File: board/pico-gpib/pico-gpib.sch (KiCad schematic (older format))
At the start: 5 parts, among them J1 GPIB, J2 USB_B_Micro, J3 RPI_GPIO, U2 SN75160BDW, U3 SN75162BDW

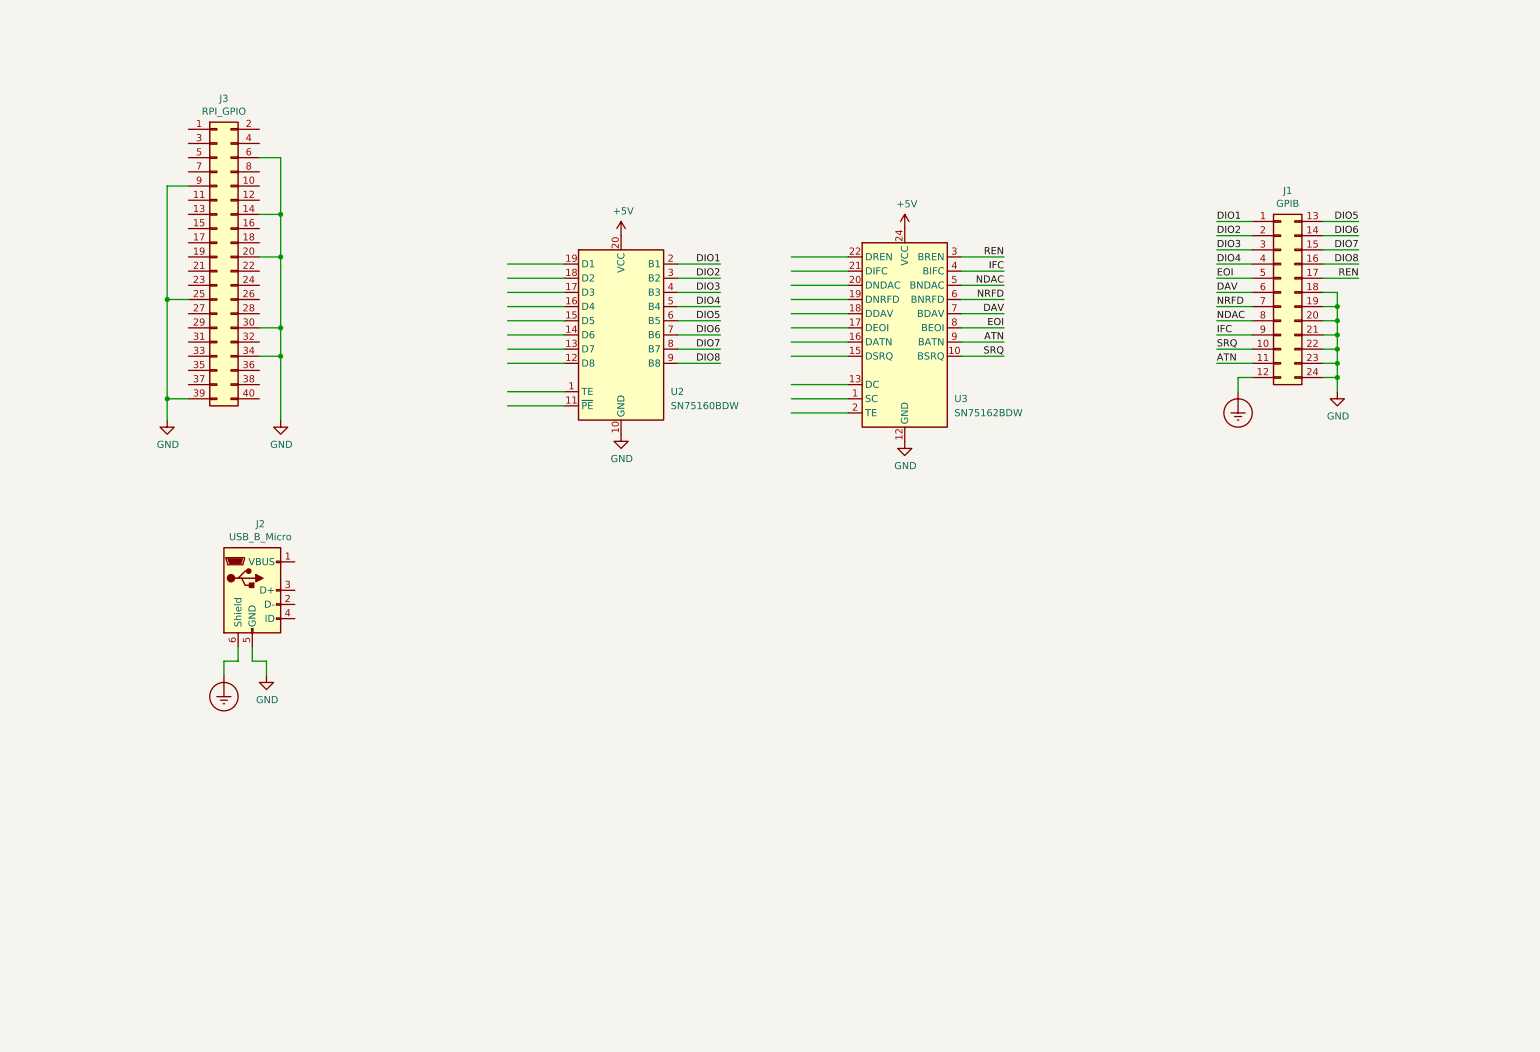
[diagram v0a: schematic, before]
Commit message: Swap connectors to top of pico board.
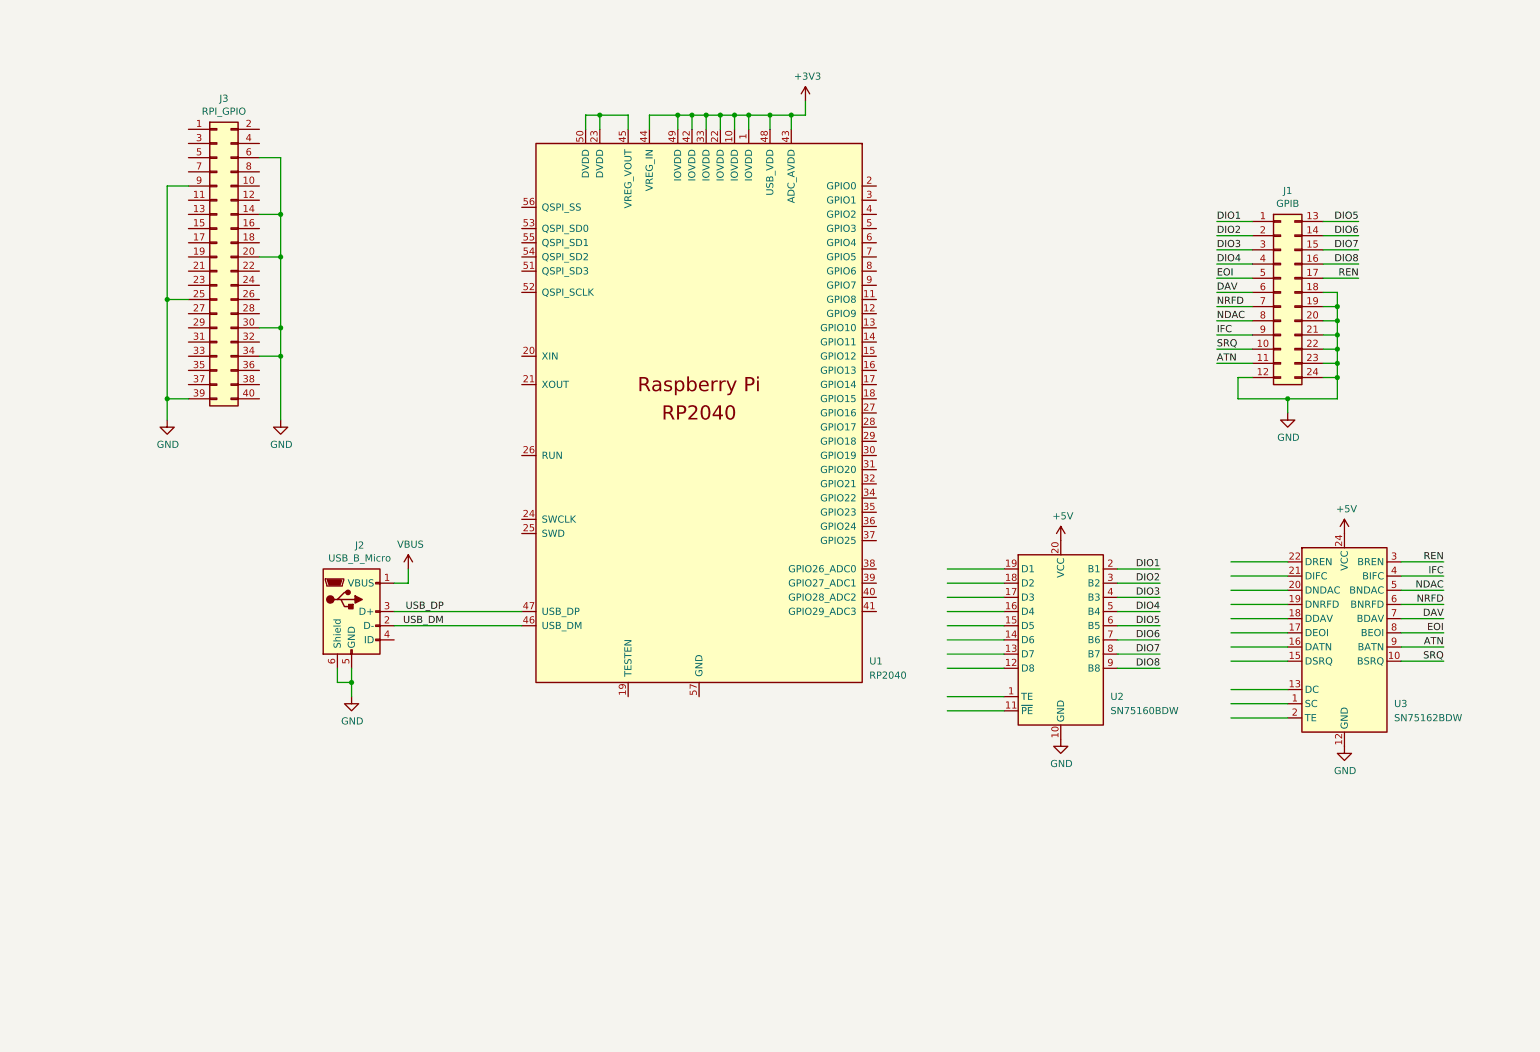
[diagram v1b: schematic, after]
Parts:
- added U1: RP2040, local:RP2040-QFN-56, symbol local:RP2040
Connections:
- net labels added: +3V3, USB_DM, USB_DP, VBUS
- net labels removed: Earth_Protective
- wire segments 91 -> 120
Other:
- moved on the sheet: J2, U2, U3

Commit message: Place and route most of the pico board.
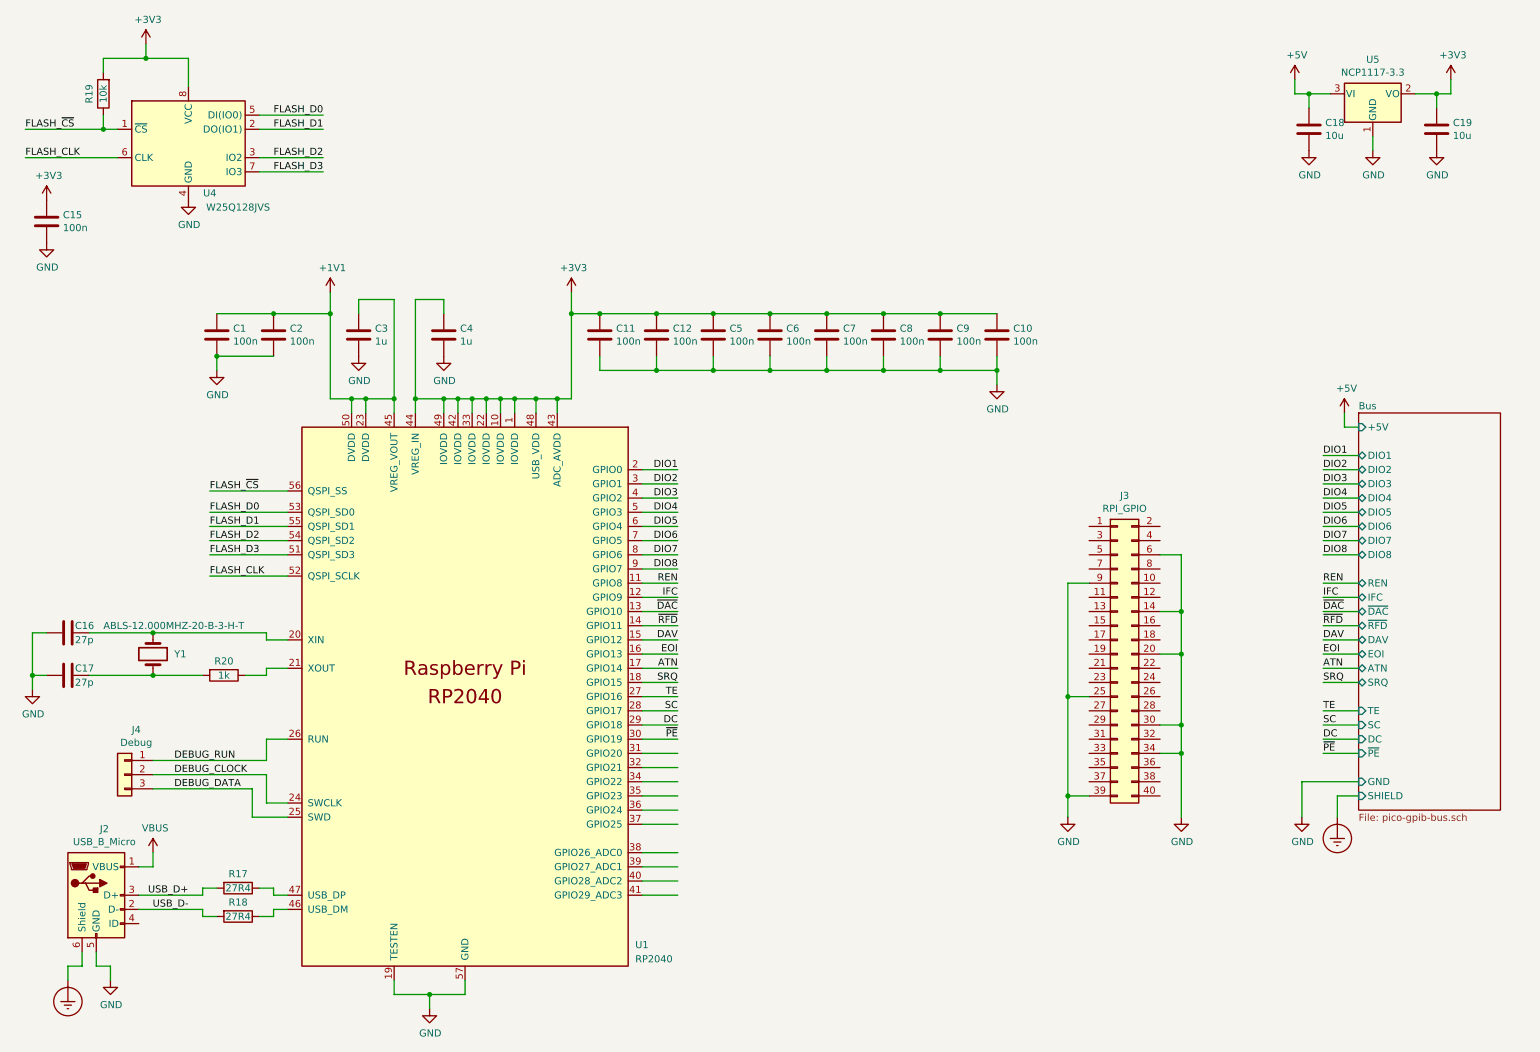
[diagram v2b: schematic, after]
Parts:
- removed J1: GPIB, local:NorComp_112-024-113R001, symbol Connector_Generic:Conn_02x12_Top_Bottom
- removed U2: SN75160BDW, Package_SO:SOIC-20W_7.5x12.8mm_P1.27mm, symbol Interface:SN75160BDW
- removed U3: SN75162BDW, Package_SO:SOIC-24W_7.5x15.4mm_P1.27mm, symbol local:SN75162BDW
- added C1, C10, C11, C12, C15, C2, C5, C6, C7, C8, C9: 100n, Capacitor_SMD:C_0402_1005Metric, symbol Device:C
- added C16, C17: 27p, Capacitor_SMD:C_0402_1005Metric, symbol Device:C
- added C18, C19: 10u, Capacitor_SMD:C_0402_1005Metric, symbol Device:C
- added C3, C4: 1u, Capacitor_SMD:C_0402_1005Metric, symbol Device:C
- added J4: Debug, Connector_PinHeader_2.54mm:PinHeader_1x03_P2.54mm_Horizontal, symbol Connector_Generic:Conn_01x03
- added R17, R18: 27R4, Resistor_SMD:R_0402_1005Metric, symbol Device:R
- added R19: 10k, Resistor_SMD:R_0402_1005Metric, symbol Device:R
- added R20: 1k, Resistor_SMD:R_0402_1005Metric, symbol Device:R
- added U4: W25Q128JVS, Package_SO:SOIC-8_5.23x5.23mm_P1.27mm, symbol Memory_Flash:W25Q128JVS
- added U5: NCP1117-3.3, Package_TO_SOT_SMD:SOT-223-3_TabPin2, symbol Regulator_Linear:NCP1117-3.3_SOT223
- added Y1: ABLS-12.000MHZ-20-B-3-H-T, Crystal:Crystal_HC49-U_Horizontal, symbol Device:Crystal
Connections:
- net labels added: +1V1, DC, DEBUG_CLOCK, DEBUG_DATA, DEBUG_RUN, Earth_Protective, FLASH_CLK, FLASH_D0, FLASH_D1, FLASH_D2, FLASH_D3, FLASH_~CS, SC, TE, USB_D+, USB_D-, ~DAC, ~PE, ~RFD
- net labels removed: NDAC, NRFD, USB_DM, USB_DP
- wire segments 120 -> 209
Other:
- moved on the sheet: J2, J3, U1

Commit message: Rotate RP2040 to fit in crystal.
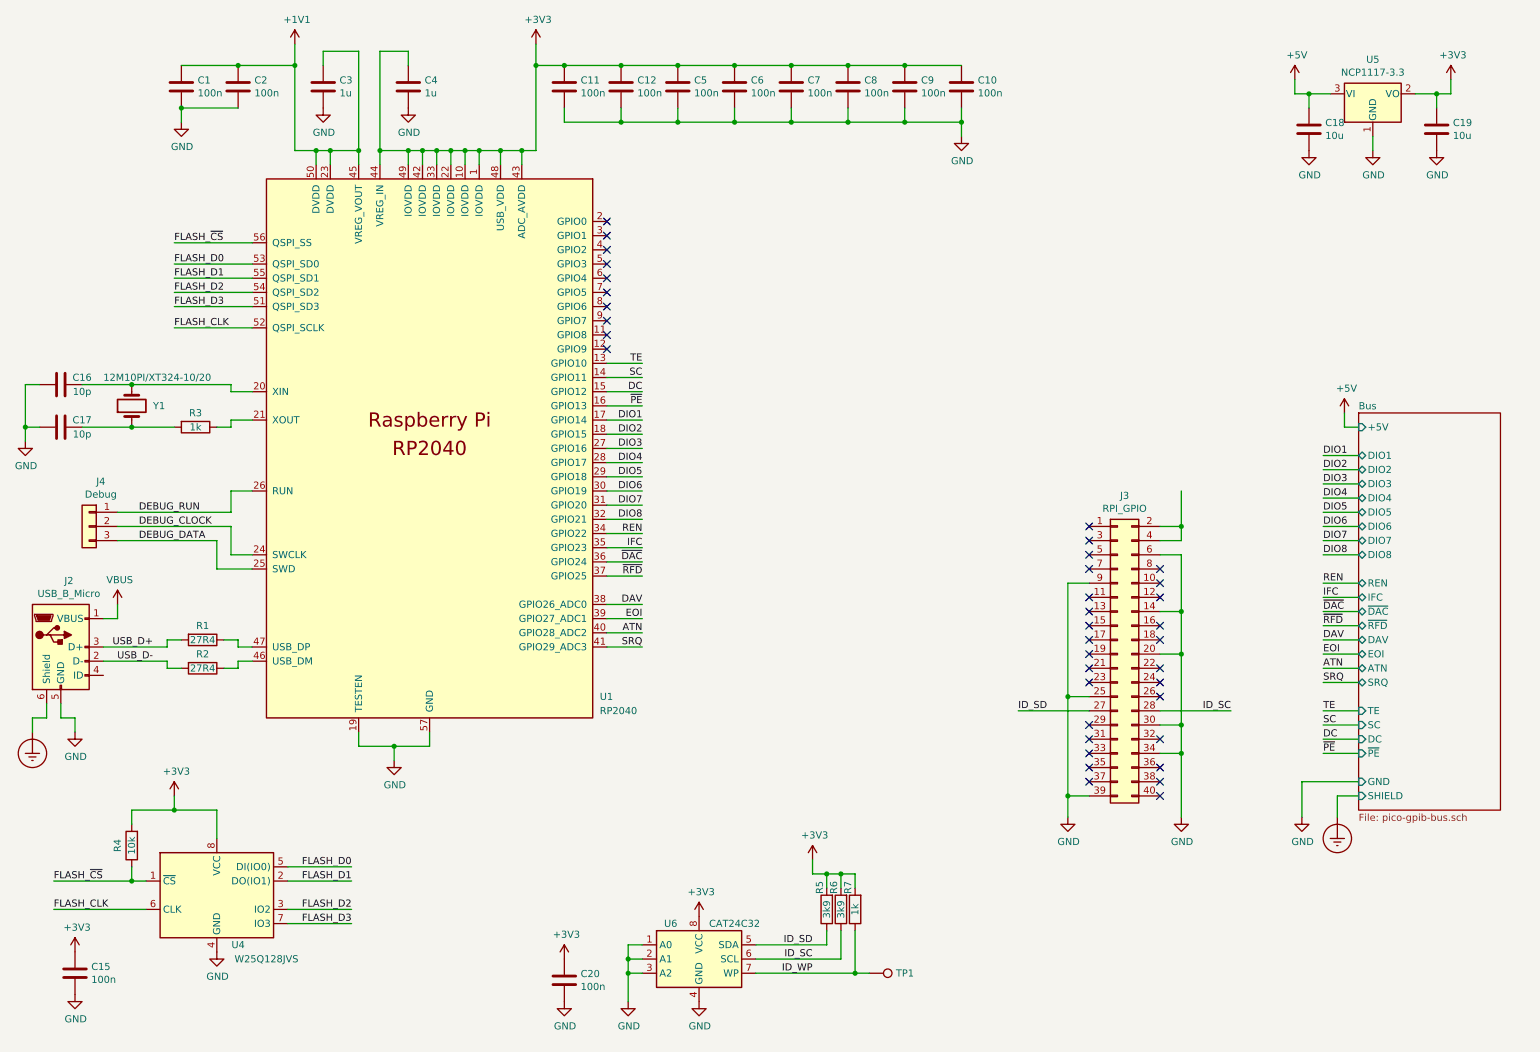
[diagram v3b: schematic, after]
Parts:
- removed R20: 1k, Resistor_SMD:R_0402_1005Metric, symbol Device:R
- added C20: 100n, Capacitor_SMD:C_0402_1005Metric, symbol Device:C
- added R3, R7: 1k, Resistor_SMD:R_0402_1005Metric, symbol Device:R
- added R5, R6: 3k9, Resistor_SMD:R_0402_1005Metric, symbol Device:R
- added TP1: TestPoint, TestPoint:TestPoint_Pad_D1.0mm, symbol Connector:TestPoint
- added U6: CAT24C32, Package_SO:SOIC-8_3.9x4.9mm_P1.27mm, symbol Memory_EEPROM:CAT24C128
- C16, C17: value 27p -> 10p
- J4: footprint Connector_PinHeader_2.54mm:PinHeader_1x03_P2.54mm_Horizontal -> Connector_PinHeader_2.54mm:PinHeader_1x03_P2.54mm_Vertical
- Y1: value ABLS-12.000MHZ-20-B-3-H-T -> 12M10PI/XT324-10/20; footprint Crystal:Crystal_HC49-U_Horizontal -> Crystal:Crystal_SMD_3225-4Pin_3.2x2.5mm
- renumbered R17 to R1, R18 to R2, R19 to R4
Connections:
- net labels added: ID_SC, ID_SD, ID_WP
- wire segments 209 -> 225
- no-connect marks 0 -> 38
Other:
- moved on the sheet: C1, C10, C11, C12, C15, C2, C3, C4, C5, C6, C7, C8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

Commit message: Route more stuff.
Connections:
- net DEBUG_CLOCK: now also J4.3 (Pin_3); no longer J4.2 (Pin_2)
- net DEBUG_DATA: now also J4.1 (Pin_1); no longer J4.3 (Pin_3)
- net GND: now also J4.2 (Pin_2)
- net DEBUG_RUN: no longer names the net of U1.26 (RUN)
- net DEBUG_RUN: no longer J4.1 (Pin_1)
- no-connect marks 38 -> 40
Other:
- moved on the sheet: J4
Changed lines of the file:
@@
 L Connector_Generic:Conn_01x03 J4
 U 1 1 62CF48E1
-P 1050 4150
-F 0 "J4" H 968 4467 50  0000 C CNN
-F 1 "Debug" H 968 4376 50  0000 C CNN
-F 2 "Connector_PinHeader_2.54mm:PinHeader_1x03_P2.54mm_Vertical" H 1050 4150 50  0001 C CNN
-F 3 "~" H 1050 4150 50  0001 C CNN
-	1    1050 4150
+P 1000 4000
+F 0 "J4" H 918 4317 50  0000 C CNN
+F 1 "Debug" H 918 4226 50  0000 C CNN
+F 2 "Connector_PinHeader_2.54mm:PinHeader_1x03_P2.54mm_Vertical" H 1000 4000 50  0001 C CNN
+F 3 "~" H 1000 4000 50  0001 C CNN
+	1    1000 4000
 	-1   0    0    -1
 $EndComp
-Wire Wire Line
-	1250 4050 2050 4050
-Wire Wire Line
-	2050 4050 2050 3900
-Wire Wire Line
-	2050 3900 2200 3900
-Wire Wire Line
-	1250 4150 2050 4150
-Wire Wire Line
-	2050 4150 2050 4350
-Wire Wire Line
-	2050 4350 2200 4350
-Wire Wire Line
-	1250 4250 1950 4250
-Wire Wire Line
-	1950 4250 1950 4450
-Wire Wire Line
-	1950 4450 2200 4450
-Text Label 1400 4050 0    50   ~ 0
-DEBUG_RUN
-Text Label 1400 4150 0    50   ~ 0
+Text Label 1350 4100 0    50   ~ 0
 DEBUG_CLOCK
-Text Label 1400 4250 0    50   ~ 0
+Text Label 1350 3900 0    50   ~ 0
 DEBUG_DATA
 $Comp
@@
 	1    0    0    -1
 $EndComp
+$Comp
+L power:GND #PWR0129
+U 1 1 635248E2
+P 1300 4200
+F 0 "#PWR0129" H 1300 3950 50  0001 C CNN
+F 1 "GND" H 1305 4027 50  0000 C CNN
+F 2 "" H 1300 4200 50  0001 C CNN
+F 3 "" H 1300 4200 50  0001 C CNN
+	1    1300 4200
+	1    0    0    -1
+$EndComp
+Wire Wire Line
+	1200 4000 1300 4000
+Wire Wire Line
+	1300 4000 1300 4200
+Wire Wire Line
+	1950 3900 1950 4450
+Wire Wire Line
+	1950 4450 2200 4450
+Wire Wire Line
+	1200 3900 1950 3900
+Wire Wire Line
+	1200 4100 2050 4100
+Wire Wire Line
+	2050 4100 2050 4350
+Wire Wire Line
+	2050 4350 2200 4350
+NoConn ~ 2200 3900
+NoConn ~ 1150 5200
 $EndSCHEMATC

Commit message: Add labels and test points.
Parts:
- added TP2, TP3, TP5: TestPoint, TestPoint:TestPoint_Pad_D1.0mm, symbol Connector:TestPoint
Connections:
- net +3V3: now also TP3.1
- net +5V: now also TP2.1
- net GND: now also TP5.1
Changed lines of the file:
@@
 L power:GND #PWR0120
 U 1 1 628CB231
-P 10100 1500
-F 0 "#PWR0120" H 10100 1250 50  0001 C CNN
-F 1 "GND" H 10105 1327 50  0000 C CNN
-F 2 "" H 10100 1500 50  0001 C CNN
-F 3 "" H 10100 1500 50  0001 C CNN
-	1    10100 1500
+P 10100 1650
+F 0 "#PWR0120" H 10100 1400 50  0001 C CNN
+F 1 "GND" H 10105 1477 50  0000 C CNN
+F 2 "" H 10100 1650 50  0001 C CNN
+F 3 "" H 10100 1650 50  0001 C CNN
+	1    10100 1650
 	1    0    0    -1
 $EndComp
@@
 NoConn ~ 2200 3900
 NoConn ~ 1150 5200
+Connection ~ 9550 1100
+Wire Wire Line
+	9450 1100 9550 1100
+$Comp
+L Connector:TestPoint TP2
+U 1 1 6374717A
+P 9450 1100
+F 0 "TP2" V 9553 1172 50  0000 C CNN
+F 1 "TestPoint" V 9554 1172 50  0001 C CNN
+F 2 "TestPoint:TestPoint_Pad_D1.0mm" H 9650 1100 50  0001 C CNN
+F 3 "~" H 9650 1100 50  0001 C CNN
+	1    9450 1100
+	0    -1   -1   0
+$EndComp
+$Comp
+L Connector:TestPoint TP3
+U 1 1 637687B0
+P 10750 1100
+F 0 "TP3" V 10650 1150 50  0000 L CNN
+F 1 "TestPoint" V 10854 1172 50  0001 C CNN
+F 2 "TestPoint:TestPoint_Pad_D1.0mm" H 10950 1100 50  0001 C CNN
+F 3 "~" H 10950 1100 50  0001 C CNN
+	1    10750 1100
+	0    1    1    0
+$EndComp
+Wire Wire Line
+	10750 1100 10650 1100
+Connection ~ 10650 1100
+$Comp
+L Connector:TestPoint TP5
+U 1 1 63801385
+P 10100 1500
+F 0 "TP5" V 10000 1550 50  0000 L CNN
+F 1 "TestPoint" V 10204 1572 50  0001 C CNN
+F 2 "TestPoint:TestPoint_Pad_D1.0mm" H 10300 1500 50  0001 C CNN
+F 3 "~" H 10300 1500 50  0001 C CNN
+	1    10100 1500
+	0    1    1    0
+$EndComp
+Connection ~ 10100 1500
+Wire Wire Line
+	10100 1500 10100 1650
 $EndSCHEMATC
